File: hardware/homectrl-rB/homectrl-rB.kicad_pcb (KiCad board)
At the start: 4 copper layers, 134 x 84.3 mm, 122 parts, among them J1 Barrel_Jack, J2 USB_C_Female_USB2_Small, J3 SMS-CONN-0, J4 SMS-CONN-1, J5 ALS_CONN, J6 PUMP0-CONN, J7 PUMP1-CONN, J8 STEP-CONN, Q1 DMP6023LE-13, Q2 AO3400A, Q3 AO3400A, SW1 SW_RESET, SW2 SW_BOOT, U1 ESP32-S3-WROOM-1, U2 TPS5405DR, U3 ID_LM66100DCKR, U4 ID_LM66100DCKR, U5 ADS1115IDGS, U6 SI2301, U7 SI2301, U8 TMC2209

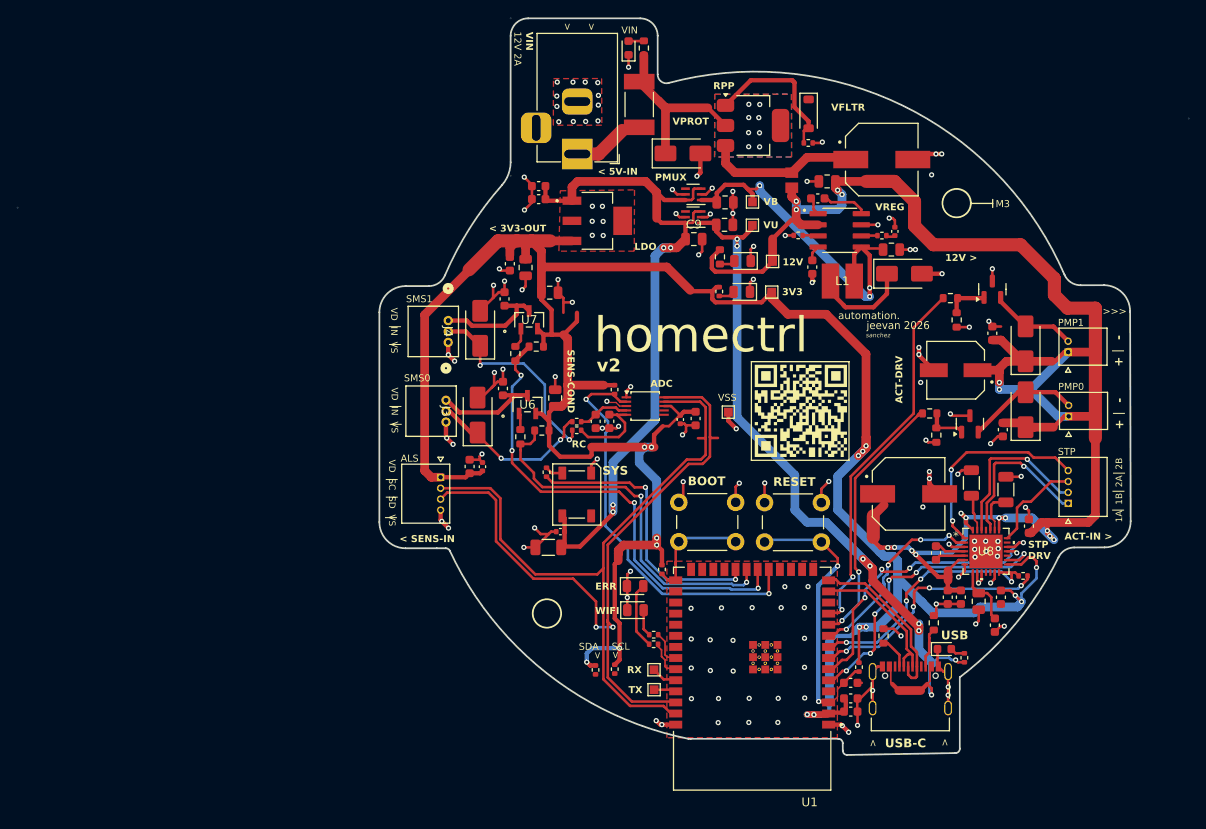
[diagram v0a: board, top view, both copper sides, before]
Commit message: review, add vias & ground pour
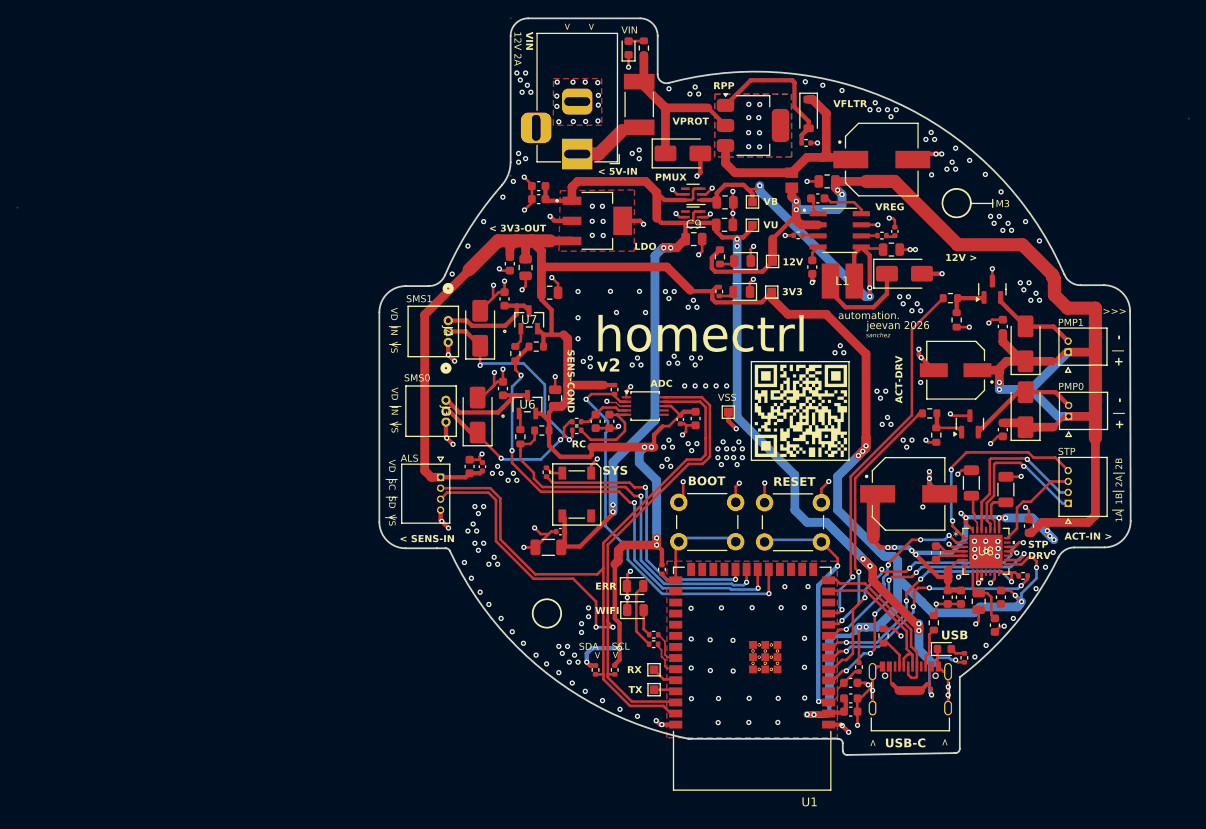
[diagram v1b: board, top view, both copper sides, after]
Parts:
- moved C42 1.43 mm to (149.4, 80.6)
- moved R2 0.25 mm to (126.9, 59.6)
- moved R13 0.09 mm to (105.0, 119.9)
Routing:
- net Net-(D3-K): track 18.6 -> 26.5 mm
- net GND: track 170.9 -> 174.1 mm, vias 130 -> 303
- net +3V3: track 295.9 -> 292.8 mm
- net +12V: track 201.9 -> 201.0 mm
- added copper zone on In1.Cu, net GND
- added copper zone on In2.Cu, net GND

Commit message: finalizing changes
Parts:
- moved F1 0.20 mm to (107.6, 55.2)
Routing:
- net GND: track 174.1 -> 176.8 mm, vias 303 -> 313
- net Net-(D3-A): track 16.9 -> 15.1 mm
- net +12V: track 201.0 -> 201.8 mm
- net +3V3: track 292.8 -> 293.6 mm
- net Net-(D2-A1): vias 14 -> 8
- net (no net): vias 1 -> 0
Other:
- board text added: "PCB: 4L FR4, 1.6mm, HASL PWR: 12VDC, 2A"
- board text removed: "*****"
- board text removed: "PCB: 4L FR4, 1.6mm, HASL PWR: 12VDC, 2A MCU: ESP32-S3"
